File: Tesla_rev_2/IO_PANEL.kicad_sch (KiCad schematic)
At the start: 10 parts, among them SW2 SW_Push, SW3 SW_Push, SW4 SW_Push, SW5 SW_Push, SW6 SW_Push, U4 NHD-C0220BIZ

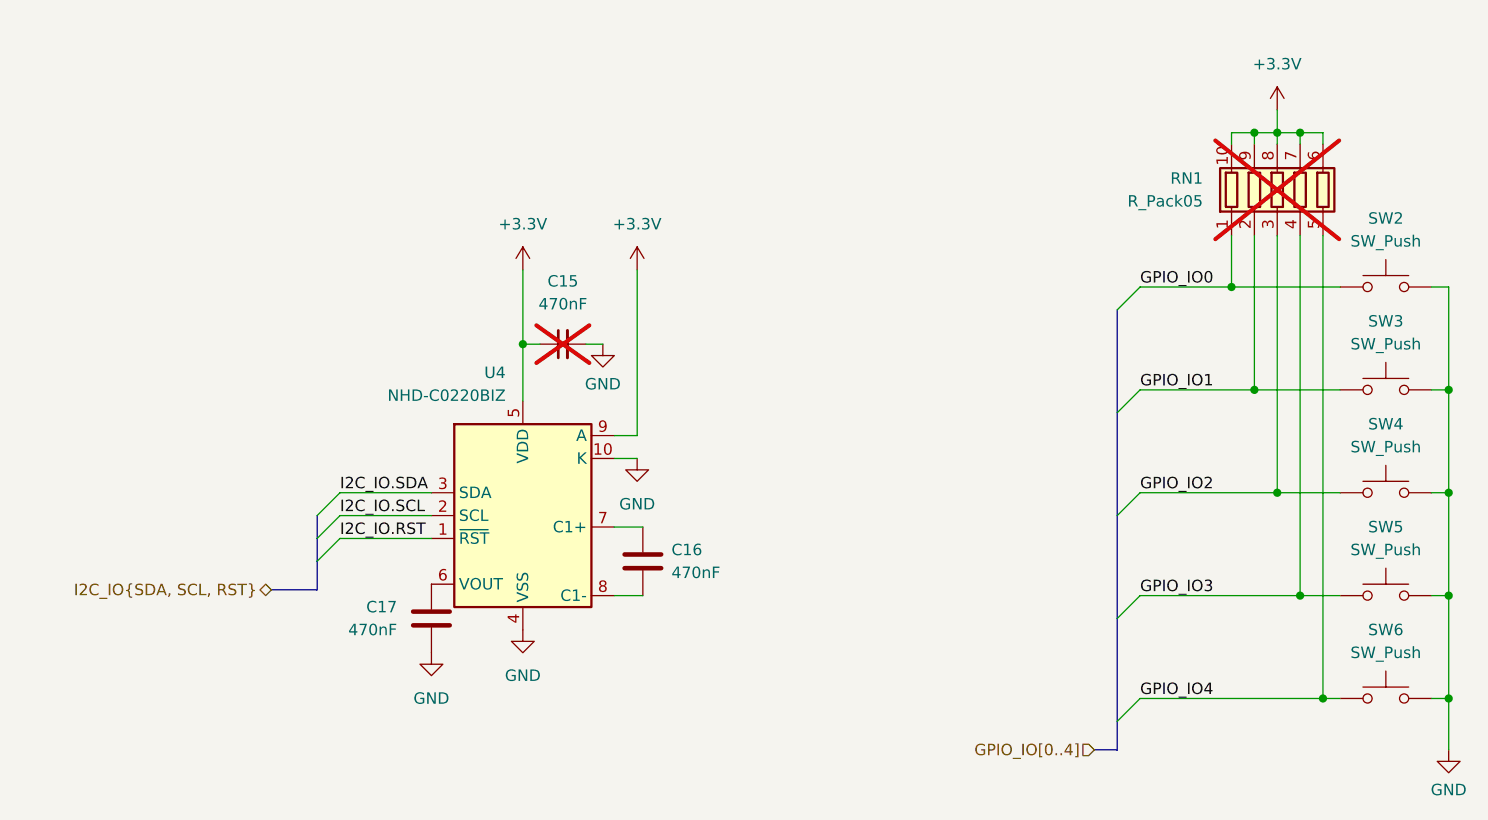
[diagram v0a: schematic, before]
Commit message: Netclasses, part Nums, LPF adjust
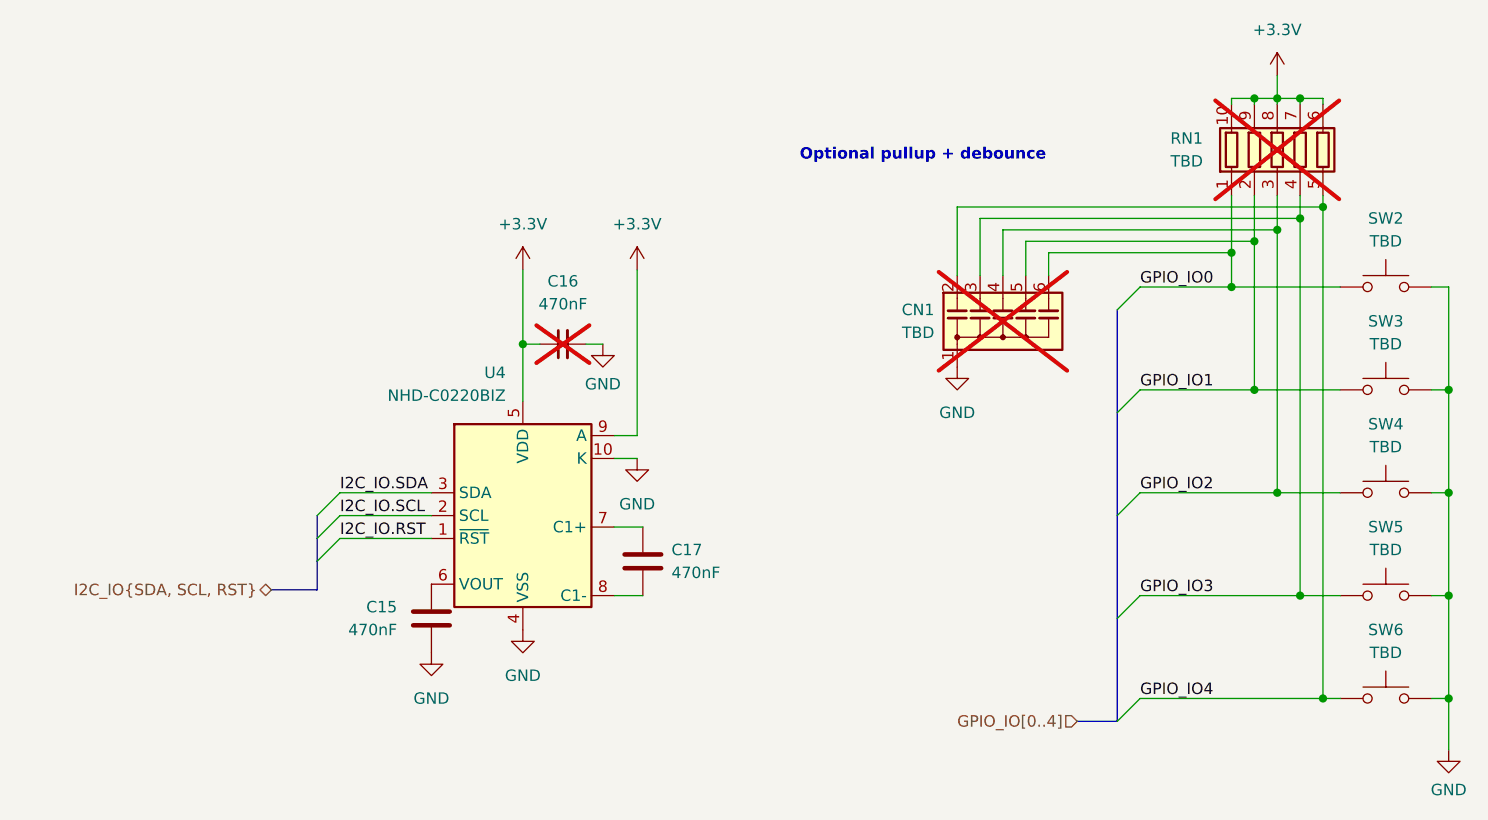
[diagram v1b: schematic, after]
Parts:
- added CN1: TBD, symbol Device:C_Network05
- RN1: value R_Pack05 -> TBD
- SW2, SW3, SW4, SW5, SW6: value SW_Push -> TBD
- renumbered C17 to C15, C15 to C16, C16 to C17
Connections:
- net GND: now also CN1.1 (common)
- net GPIO_IO0: now also CN1.6 (C5)
- net GPIO_IO1: now also CN1.5 (C4)
- net GPIO_IO2: now also CN1.4 (C3)
- net GPIO_IO3: now also CN1.3 (C2)
- net GPIO_IO4: now also CN1.2 (C1)
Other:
- note added: "Optional pullup + debounce"
- title: (none) -> Tesla sextant BT
- moved on the sheet: RN1
